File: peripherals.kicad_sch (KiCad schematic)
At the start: 28 parts, among them J4 Conn_01x04, J5 Conn_01x06, J6 Conn_01x06, U5 LSM6DSV, U6 TB67H450FNG_EL, U7 TB67H450FNG_EL

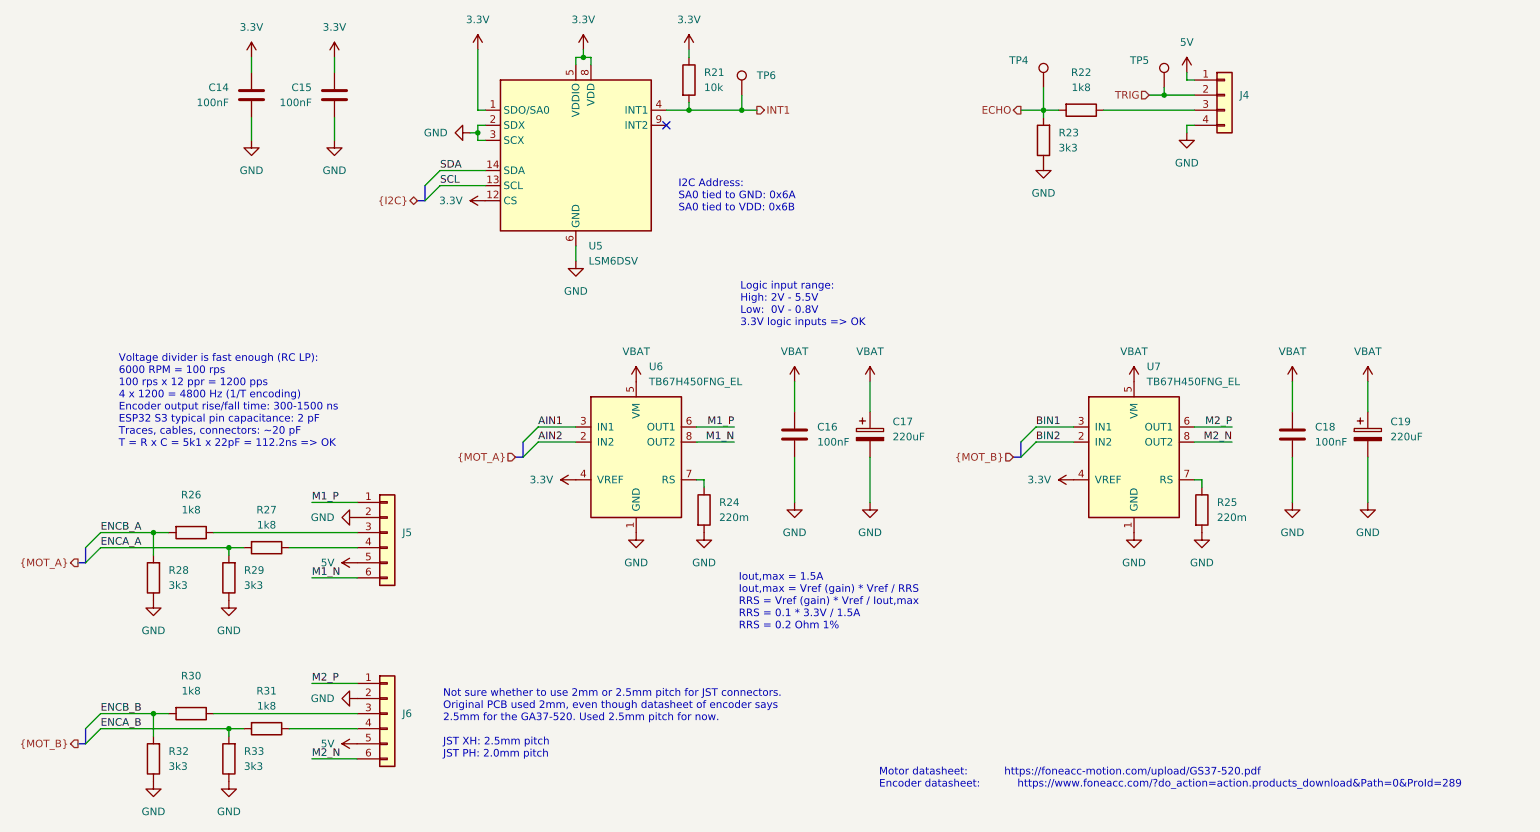
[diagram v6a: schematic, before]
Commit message: Document strapping pins
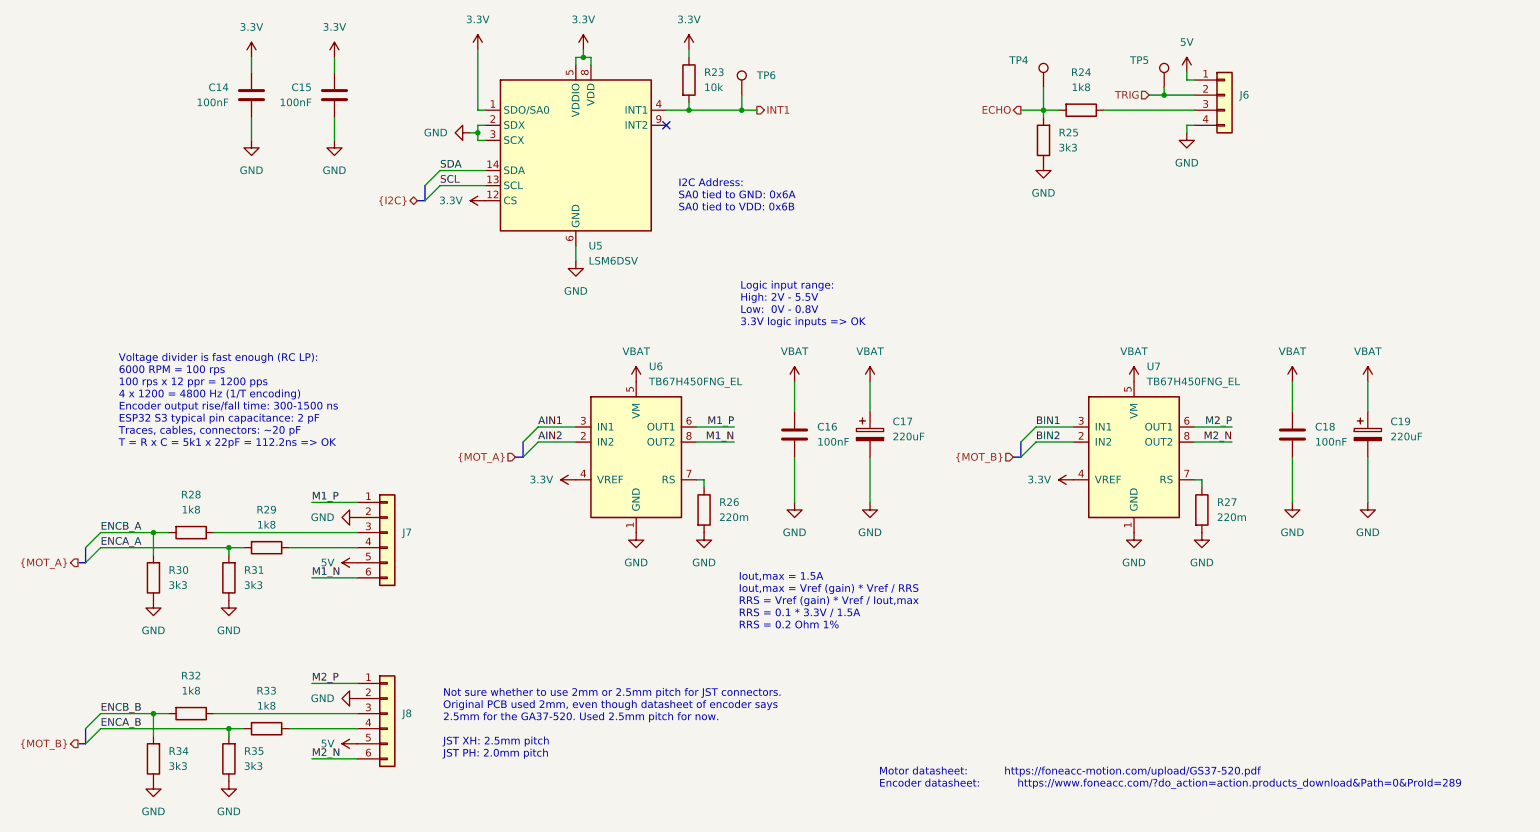
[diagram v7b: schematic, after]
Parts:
- renumbered J4 to J6, J5 to J7, J6 to J8, R21 to R23, R22 to R24, R23 to R25, R24 to R26, R25 to R27, R26 to R28, R27 to R29, R28 to R30, R29 to R31, R30 to R32, R31 to R33, R32 to R34, R33 to R35

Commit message: Connect remaining tracks
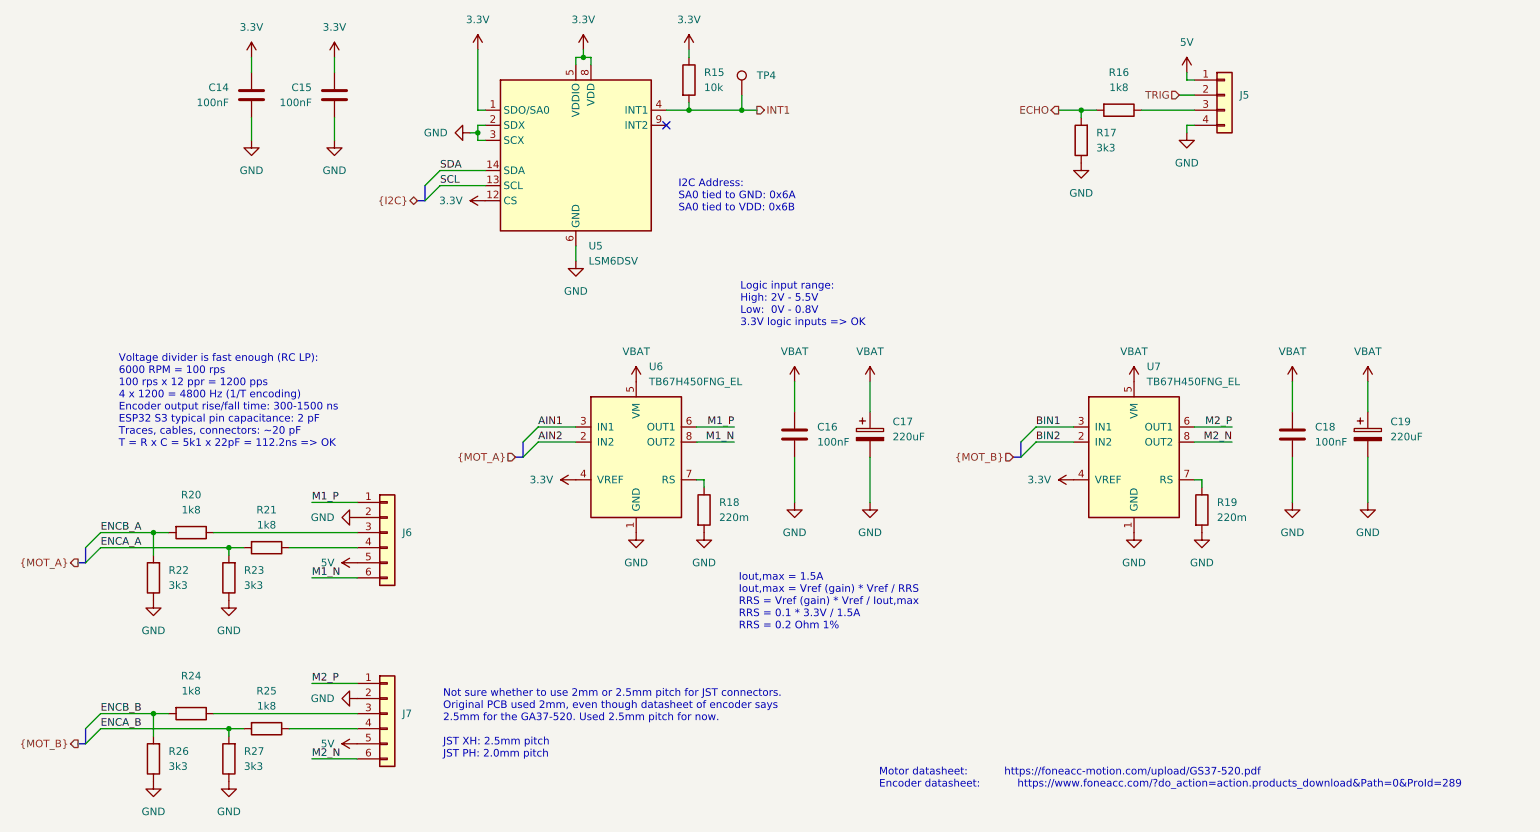
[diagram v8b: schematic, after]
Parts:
- removed TP4, TP5: TestPoint, TestPoint:TestPoint_THTPad_D1.0mm_Drill0.5mm, symbol Connector:TestPoint
- renumbered J6 to J5, J7 to J6, J8 to J7, R23 to R15, R24 to R16, R25 to R17, R26 to R18, R27 to R19, R28 to R20, R29 to R21, R30 to R22, R31 to R23, R32 to R24, R33 to R25, R34 to R26, R35 to R27, TP6 to TP4
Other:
- moved on the sheet: R16, R17
